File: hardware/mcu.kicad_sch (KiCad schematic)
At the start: 56 parts, among them J10 PRPC001DAAN-RC, J11 PRPC006SAAN-RC, J12 PRPC004SAAN-RC, J8 SBH11-NBPC-D05-SM-BK, J9 PRPC006SAAN-RC, U5 AT25SF081B-SSHD-B, U6 MCP9808T-E/MS, U7 STM32L552CET6, Y1 ABS05-32.768KHZ-9-T, Y2 ECS-160-9-37-CKM-TR3

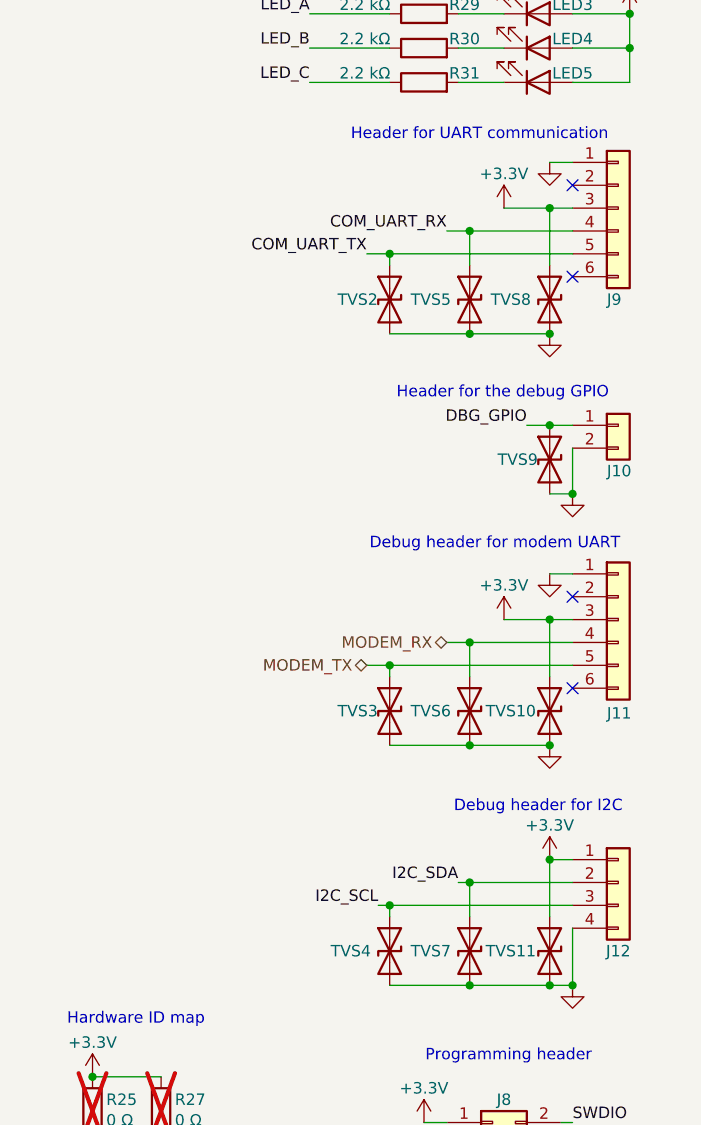
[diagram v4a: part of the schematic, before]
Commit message: HW: Disconnect +3V3 from UART/Modem header
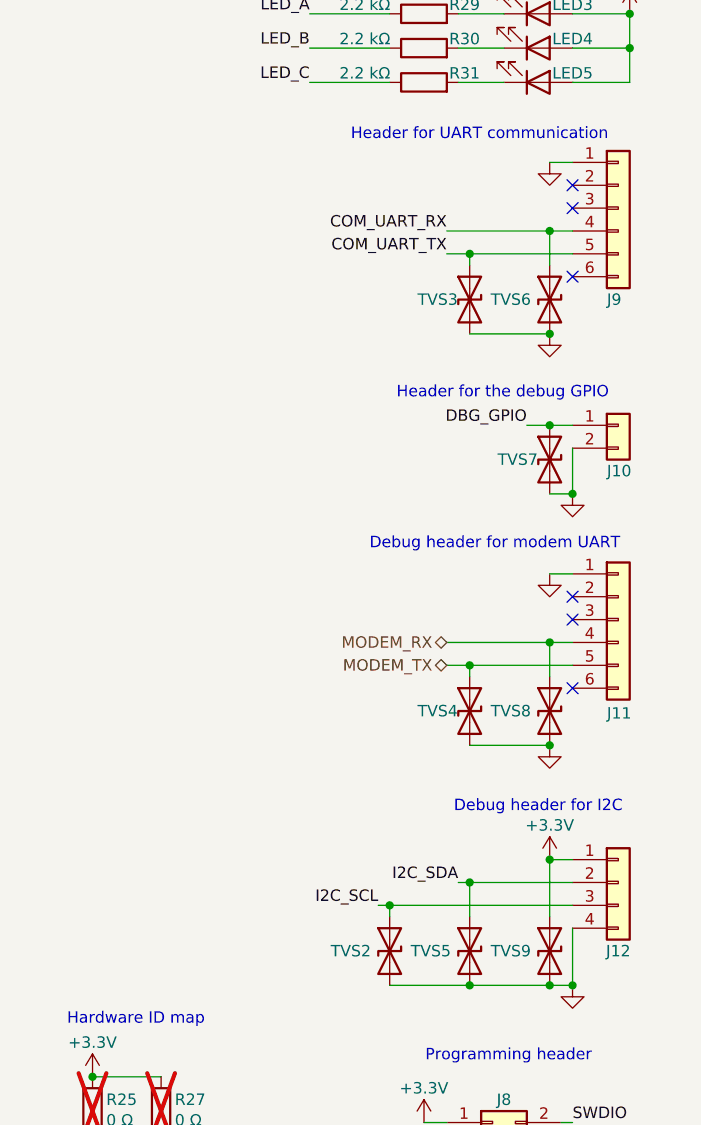
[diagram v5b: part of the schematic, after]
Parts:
- removed TVS10, TVS8: D5V0F1B2WS-7, Diode_SMD:D_SOD-323_HandSoldering, symbol Device:D_TVS
- renumbered TVS4 to TVS2, TVS2 to TVS3, TVS3 to TVS4, TVS7 to TVS5, TVS5 to TVS6, TVS9 to TVS7, TVS6 to TVS8, TVS11 to TVS9
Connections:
- net +3.3V: no longer J11.3 (Pin_3), J9.3 (Pin_3)
- no-connect marks 15 -> 17
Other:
- moved on the sheet: TVS3, TVS4, TVS6, TVS8

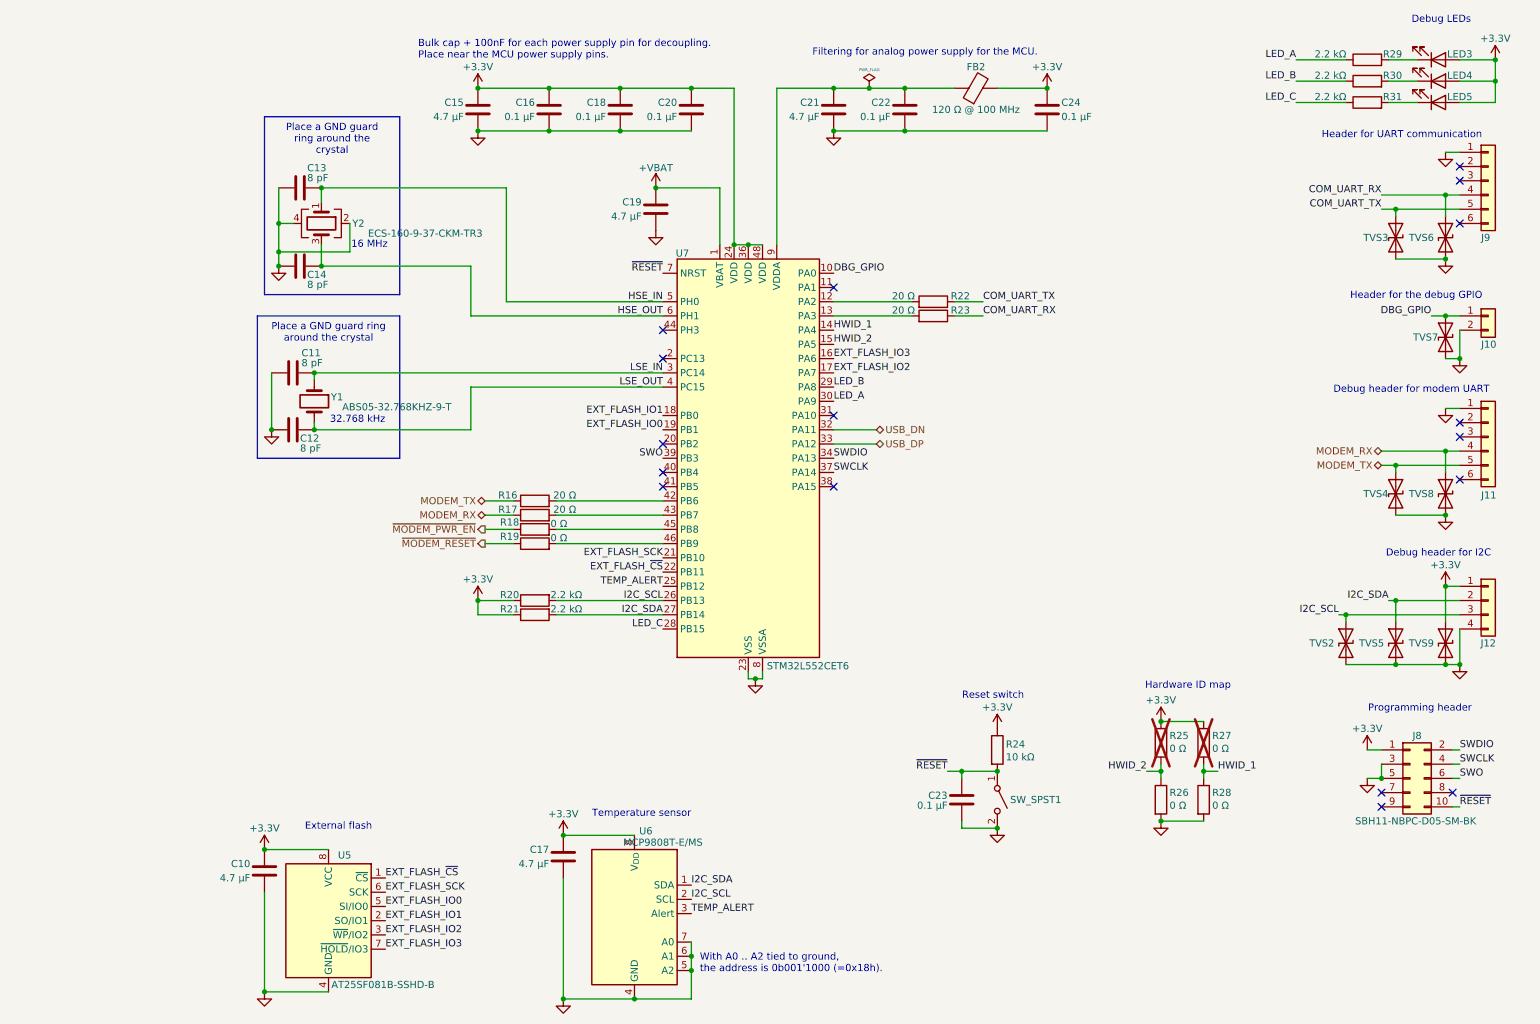
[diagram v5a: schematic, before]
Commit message: HW: Replace buck reg with buck-boost reg
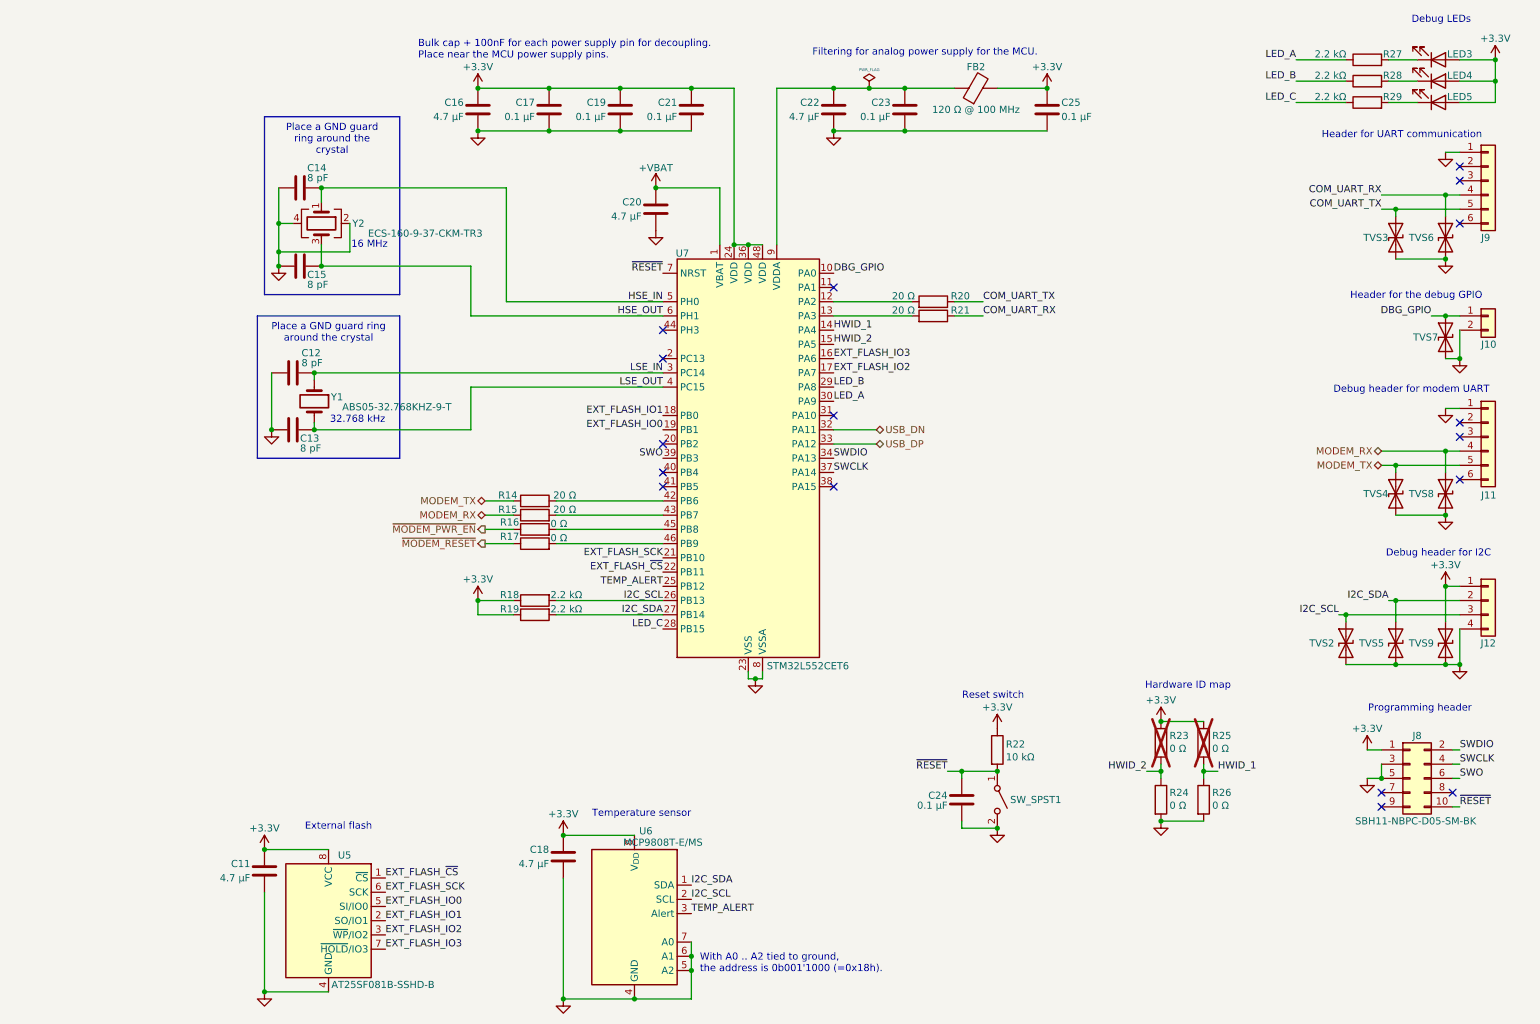
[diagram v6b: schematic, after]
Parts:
- renumbered C10 to C11, C11 to C12, C12 to C13, C13 to C14, C14 to C15, C15 to C16, C16 to C17, C17 to C18, C18 to C19, C19 to C20, C20 to C21, C21 to C22, C22 to C23, C23 to C24, C24 to C25, R16 to R14, R17 to R15, R18 to R16, R19 to R17, R20 to R18, R21 to R19, R22 to R20, R23 to R21, R24 to R22, R25 to R23, R26 to R24, R27 to R25, R28 to R26, R29 to R27, R30 to R28, R31 to R29
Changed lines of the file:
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@@
 		(on_board yes)
 		(dnp yes)
-		(property "Reference" "R25"
+		(property "Reference" "R23"
 			(at 222.504 144.78 0)
 			(effects
@@
 			(project "iida_devkit"
 				(path "/b12a6e25-97fb-4aba-bc96-af8db389bb9a/6dd8d741-3080-458c-a4f5-a05a3905bb8a"
-					(reference "R25")
+					(reference "R23")
 					(unit 1)
 				)
@@
 		(on_board yes)
 		(dnp no)
-		(property "Reference" "C22"
+		(property "Reference" "C23"
 			(at 172.72 31.75 0)
 			(effects
@@
 			(project "iida_devkit"
 				(path "/b12a6e25-97fb-4aba-bc96-af8db389bb9a/6dd8d741-3080-458c-a4f5-a05a3905bb8a"
-					(reference "C22")
+					(reference "C23")
 					(unit 1)
 				)
@@
 		(on_board yes)
 		(dnp no)
-		(property "Reference" "C21"
+		(property "Reference" "C22"
 			(at 160.02 31.75 0)
 			(effects
@@
 			(project "iida_devkit"
 				(path "/b12a6e25-97fb-4aba-bc96-af8db389bb9a/6dd8d741-3080-458c-a4f5-a05a3905bb8a"
-					(reference "C21")
+					(reference "C22")
 					(unit 1)
 				)
@@
 		(on_board yes)
 		(dnp no)
-		(property "Reference" "R17"
+		(property "Reference" "R15"
 			(at 104.394 104.394 90)
 			(effects
@@
 			(project "iida_devkit"
 				(path "/b12a6e25-97fb-4aba-bc96-af8db389bb9a/6dd8d741-3080-458c-a4f5-a05a3905bb8a"
-					(reference "R17")
+					(reference "R15")
 					(unit 1)
 				)
@@
 		(on_board yes)
 		(dnp no)
-		(property "Reference" "R26"
+		(property "Reference" "R24"
 			(at 222.504 154.94 0)
 			(effects
@@
 			(project "iida_devkit"
 				(path "/b12a6e25-97fb-4aba-bc96-af8db389bb9a/6dd8d741-3080-458c-a4f5-a05a3905bb8a"
-					(reference "R26")
+					(reference "R24")
 					(unit 1)
 				)
@@
 		(on_board yes)
 		(dnp no)
-		(property "Reference" "C17"
+		(property "Reference" "C18"
 			(at 111.76 165.1 0)
 			(effects
@@
 			(project "iida_devkit"
 				(path "/b12a6e25-97fb-4aba-bc96-af8db389bb9a/6dd8d741-3080-458c-a4f5-a05a3905bb8a"
-					(reference "C17")
+					(reference "C18")
 					(unit 1)
 				)
@@
 		(on_board yes)
 		(dnp no)
-		(property "Reference" "R22"
+		(property "Reference" "R20"
 			(at 185.166 66.294 90)
 			(effects
@@
 			(project "iida_devkit"
 				(path "/b12a6e25-97fb-4aba-bc96-af8db389bb9a/6dd8d741-3080-458c-a4f5-a05a3905bb8a"
-					(reference "R22")
+					(reference "R20")
 					(unit 1)
 				)
@@
 		(on_board yes)
 		(dnp no)
-		(property "Reference" "C15"
+		(property "Reference" "C16"
 			(at 96.52 31.75 0)
 			(effects
@@
 			(project "iida_devkit"
 				(path "/b12a6e25-97fb-4aba-bc96-af8db389bb9a/6dd8d741-3080-458c-a4f5-a05a3905bb8a"
-					(reference "C15")
+					(reference "C16")
 					(unit 1)
 				)
@@
 		(on_board yes)
 		(dnp no)
-		(property "Reference" "R18"
+		(property "Reference" "R16"
 			(at 106.426 106.68 90)
 			(effects
@@
 			(project "iida_devkit"
 				(path "/b12a6e25-97fb-4aba-bc96-af8db389bb9a/6dd8d741-3080-458c-a4f5-a05a3905bb8a"
-					(reference "R18")
+					(reference "R16")
 					(unit 1)
 				)
@@
 		(on_board yes)
 		(dnp no)
-		(property "Reference" "C16"
+		(property "Reference" "C17"
 			(at 109.22 31.75 0)
 			(effects
@@
 			(project "iida_devkit"
 				(path "/b12a6e25-97fb-4aba-bc96-af8db389bb9a/6dd8d741-3080-458c-a4f5-a05a3905bb8a"
-					(reference "C16")
+					(reference "C17")
 					(unit 1)
 				)
@@
 		(on_board yes)
 		(dnp no)
-		(property "Reference" "C10"
+		(property "Reference" "C11"
 			(at 58.42 167.64 0)
 			(effects
@@
 			(project "iida_devkit"
 				(path "/b12a6e25-97fb-4aba-bc96-af8db389bb9a/6dd8d741-3080-458c-a4f5-a05a3905bb8a"
-					(reference "C10")
+					(reference "C11")
 					(unit 1)
 				)
@@
 		(on_board yes)
 		(dnp no)
-		(property "Reference" "R30"
+		(property "Reference" "R28"
 			(at 260.604 26.924 90)
 			(effects
@@
 			(project "iida_devkit"
 				(path "/b12a6e25-97fb-4aba-bc96-af8db389bb9a/6dd8d741-3080-458c-a4f5-a05a3905bb8a"
-					(reference "R30")
+					(reference "R28")
 					(unit 1)
 				)
@@
 		(on_board yes)
 		(dnp no)
-		(property "Reference" "R16"
+		(property "Reference" "R14"
 			(at 104.394 101.854 90)
 			(effects
@@
 			(project ""
 				(path "/b12a6e25-97fb-4aba-bc96-af8db389bb9a/6dd8d741-3080-458c-a4f5-a05a3905bb8a"
-					(reference "R16")
+					(reference "R14")
 					(unit 1)
 				)
@@
 		(on_board yes)
 		(dnp no)
-		(property "Reference" "R19"
+		(property "Reference" "R17"
 			(at 106.426 109.22 90)
 			(effects
@@
 			(project "iida_devkit"
 				(path "/b12a6e25-97fb-4aba-bc96-af8db389bb9a/6dd8d741-3080-458c-a4f5-a05a3905bb8a"
-					(reference "R19")
+					(reference "R17")
 					(unit 1)
 				)
@@
 		(on_board yes)
 		(dnp no)
-		(property "Reference" "C19"
+		(property "Reference" "C20"
 			(at 128.27 49.53 0)
 			(effects
@@
 			(project "iida_devkit"
 				(path "/b12a6e25-97fb-4aba-bc96-af8db389bb9a/6dd8d741-3080-458c-a4f5-a05a3905bb8a"
-					(reference "C19")
+					(reference "C20")
 					(unit 1)
 				)
@@
 		(on_board yes)
 		(dnp no)
-		(property "Reference" "C20"
+		(property "Reference" "C21"
 			(at 134.62 31.75 0)
 			(effects
@@
 			(project "iida_devkit"
 				(path "/b12a6e25-97fb-4aba-bc96-af8db389bb9a/6dd8d741-3080-458c-a4f5-a05a3905bb8a"
-					(reference "C20")
+					(reference "C21")
 					(unit 1)
 				)
@@
 		(on_board yes)
 		(dnp no)
-		(property "Reference" "C23"
+		(property "Reference" "C24"
 			(at 182.88 155.448 0)
 			(effects
@@
 			(project "iida_devkit"
 				(path "/b12a6e25-97fb-4aba-bc96-af8db389bb9a/6dd8d741-3080-458c-a4f5-a05a3905bb8a"
-					(reference "C23")
+					(reference "C24")
 					(unit 1)
 				)
@@
 		(on_board yes)
 		(dnp no)
-		(property "Reference" "C24"
+		(property "Reference" "C25"
 			(at 203.2 31.75 0)
 			(effects
@@
 			(project "iida_devkit"
 				(path "/b12a6e25-97fb-4aba-bc96-af8db389bb9a/6dd8d741-3080-458c-a4f5-a05a3905bb8a"
-					(reference "C24")
+					(reference "C25")
 					(unit 1)
 				)
@@
 		(on_board yes)
 		(dnp no)
-		(property "Reference" "R29"
+		(property "Reference" "R27"
 			(at 260.604 23.114 90)
 			(effects
@@
 			(project "iida_devkit"
 				(path "/b12a6e25-97fb-4aba-bc96-af8db389bb9a/6dd8d741-3080-458c-a4f5-a05a3905bb8a"
-					(reference "R29")
+					(reference "R27")
 					(unit 1)
 				)
@@
 		(on_board yes)
 		(dnp no)
-		(property "Reference" "R20"
+		(property "Reference" "R18"
 			(at 106.426 119.634 90)
 			(effects
@@
 			(project "iida_devkit"
 				(path "/b12a6e25-97fb-4aba-bc96-af8db389bb9a/6dd8d741-3080-458c-a4f5-a05a3905bb8a"
-					(reference "R20")
+					(reference "R18")
 					(unit 1)
 				)
@@
 		(on_board yes)
 		(dnp no)
-		(property "Reference" "R21"
+		(property "Reference" "R19"
 			(at 106.426 122.174 90)
 			(effects
@@
 			(project "iida_devkit"
 				(path "/b12a6e25-97fb-4aba-bc96-af8db389bb9a/6dd8d741-3080-458c-a4f5-a05a3905bb8a"
-					(reference "R21")
+					(reference "R19")
 					(unit 1)
 				)
@@
 		(on_board yes)
 		(dnp no)
-		(property "Reference" "C18"
+		(property "Reference" "C19"
 			(at 121.92 31.75 0)
 			(effects
@@
 			(project "iida_devkit"
 				(path "/b12a6e25-97fb-4aba-bc96-af8db389bb9a/6dd8d741-3080-458c-a4f5-a05a3905bb8a"
-					(reference "C18")
+					(reference "C19")
 					(unit 1)
 				)
@@
 		(on_board yes)
 		(dnp yes)
-		(property "Reference" "R27"
+		(property "Reference" "R25"
 			(at 230.124 144.78 0)
 			(effects
@@
 			(project "iida_devkit"
 				(path "/b12a6e25-97fb-4aba-bc96-af8db389bb9a/6dd8d741-3080-458c-a4f5-a05a3905bb8a"
-					(reference "R27")
+					(reference "R25")
 					(unit 1)
 				)
@@
 		(on_board yes)
 		(dnp no)
-		(property "Reference" "C12"
+		(property "Reference" "C13"
 			(at 67.31 91.694 90)
 			(effects
@@
 			(project "iida_devkit"
 				(path "/b12a6e25-97fb-4aba-bc96-af8db389bb9a/6dd8d741-3080-458c-a4f5-a05a3905bb8a"
-					(reference "C12")
+					(reference "C13")
 					(unit 1)
 				)
@@
 		(on_board yes)
 		(dnp no)
-		(property "Reference" "C13"
+		(property "Reference" "C14"
 			(at 68.58 43.434 90)
 			(effects
@@
 			(project "iida_devkit"
 				(path "/b12a6e25-97fb-4aba-bc96-af8db389bb9a/6dd8d741-3080-458c-a4f5-a05a3905bb8a"
-					(reference "C13")
+					(reference "C14")
 					(unit 1)
 				)
@@
 		(on_board yes)
 		(dnp no)
-		(property "Reference" "R24"
+		(property "Reference" "R22"
 			(at 193.294 146.304 0)
 			(effects
@@
 			(project "iida_devkit"
 				(path "/b12a6e25-97fb-4aba-bc96-af8db389bb9a/6dd8d741-3080-458c-a4f5-a05a3905bb8a"
-					(reference "R24")
+					(reference "R22")
 					(unit 1)
 				)
@@
 		(on_board yes)
 		(dnp no)
-		(property "Reference" "R31"
+		(property "Reference" "R29"
 			(at 260.604 30.734 90)
 			(effects
@@
 			(project "iida_devkit"
 				(path "/b12a6e25-97fb-4aba-bc96-af8db389bb9a/6dd8d741-3080-458c-a4f5-a05a3905bb8a"
-					(reference "R31")
+					(reference "R29")
 					(unit 1)
 				)
@@
 		(on_board yes)
 		(dnp no)
-		(property "Reference" "C11"
+		(property "Reference" "C12"
 			(at 67.564 76.454 90)
 			(effects
@@
 			(project "iida_devkit"
 				(path "/b12a6e25-97fb-4aba-bc96-af8db389bb9a/6dd8d741-3080-458c-a4f5-a05a3905bb8a"
-					(reference "C11")
+					(reference "C12")
 					(unit 1)
 				)
@@
 		(on_board yes)
 		(dnp no)
-		(property "Reference" "R28"
+		(property "Reference" "R26"
 			(at 230.124 154.94 0)
 			(effects
@@
 			(project "iida_devkit"
 				(path "/b12a6e25-97fb-4aba-bc96-af8db389bb9a/6dd8d741-3080-458c-a4f5-a05a3905bb8a"
-					(reference "R28")
+					(reference "R26")
 					(unit 1)
 				)
@@
 		(on_board yes)
 		(dnp no)
-		(property "Reference" "C14"
+		(property "Reference" "C15"
 			(at 68.58 62.484 90)
 			(effects
@@
 			(project "iida_devkit"
 				(path "/b12a6e25-97fb-4aba-bc96-af8db389bb9a/6dd8d741-3080-458c-a4f5-a05a3905bb8a"
-					(reference "C14")
+					(reference "C15")
 					(unit 1)
 				)
@@
 		(on_board yes)
 		(dnp no)
-		(property "Reference" "R23"
+		(property "Reference" "R21"
 			(at 185.166 68.834 90)
 			(effects
@@
 			(project "iida_devkit"
 				(path "/b12a6e25-97fb-4aba-bc96-af8db389bb9a/6dd8d741-3080-458c-a4f5-a05a3905bb8a"
-					(reference "R23")
+					(reference "R21")
 					(unit 1)
 				)

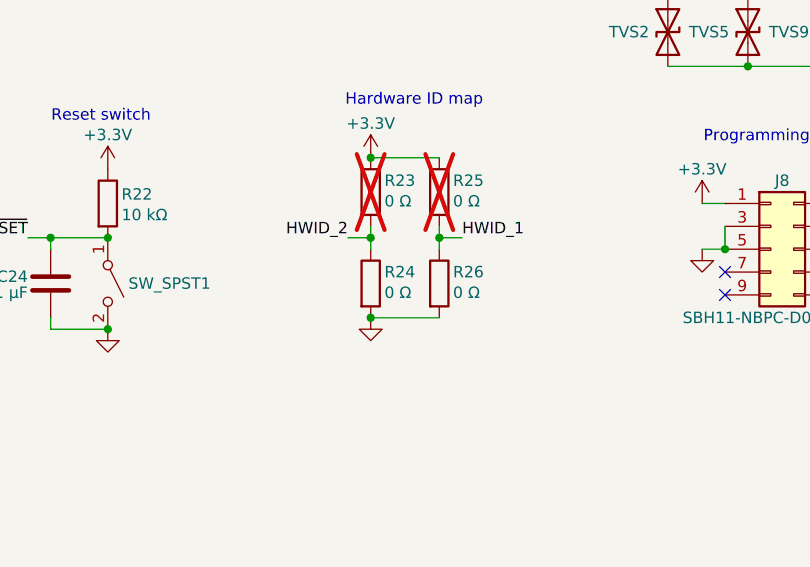
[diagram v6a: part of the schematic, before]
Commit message: HW: Refactor HWID
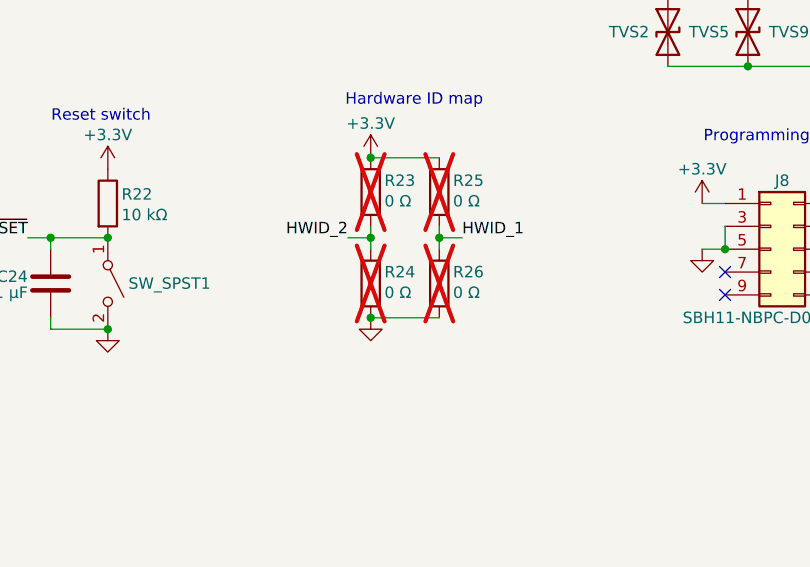
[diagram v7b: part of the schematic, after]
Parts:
- R23, R25: now in the parts list
- R24, R26: now not fitted
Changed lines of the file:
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@@
 		(unit 1)
 		(exclude_from_sim no)
-		(in_bom no)
+		(in_bom yes)
 		(on_board yes)
 		(dnp yes)
@@
 		(in_bom yes)
 		(on_board yes)
-		(dnp no)
+		(dnp yes)
 		(property "Reference" "R24"
 			(at 222.504 154.94 0)
@@
 		(unit 1)
 		(exclude_from_sim no)
-		(in_bom no)
+		(in_bom yes)
 		(on_board yes)
 		(dnp yes)
@@
 		(in_bom yes)
 		(on_board yes)
-		(dnp no)
+		(dnp yes)
 		(property "Reference" "R26"
 			(at 230.124 154.94 0)
